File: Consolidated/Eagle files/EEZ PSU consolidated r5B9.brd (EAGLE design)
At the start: 309 x 150 mm, 546 parts, among them IC1 LTC3864EMSE#PBF, IC10 REF5025AIDG4, IC11 DAC8552IDGKTG4, IC12 ADG465SOT-23, IC13 TS5A9411DCKT, IC14 ADS1120IPWR, IC15 LP339D, IC16 LM25575MH/NOPB, IC17 TPD4E002DRLR, IC18 TPD2E001DZDR, IC19 ADUM3160BRWZ, IC2 MC79L05, IC20 TLC5925IDBQR, IC21 Si8641EC-B-IS1, IC22 SI8651EC-B-IS1, IC23 SI8651EC-B-IS1, IC24 LD1117ADT33TR, IC25 Si8641EC-B-IS1, IC26 PCA21125T/Q900/1,1, IC27 AT25256B-SSHL-B, IC28 W5500, IC29 BC857BS, IC3 MC78L05, IC30 TLC555, IC31 SN74LVC2G08DCTR, IC32 TPS3705-33D, IC33 SN74LV1T34DBVR, IC34 SN74LVC2G02DCTR, IC4 LM5574MTX/NOPB, IC5 LP2951SO8, IC6 TL072D, IC7 TL072D, IC8 OP27GSZ, IC9 MCP23S08-E/SO, J1 BS-244DSM-R, J2 BS-244DSM-G, J3 BS-244DSM-B, J4 BS-244DSM-R, J5 BS-244DSM-B, Q1 SUD19P06-60, Q10 MMBT5401, Q11 MMBT5401, Q12 MMBT5551, Q13 MMBT5551, Q14 BSS84P, Q15 2N7002, Q16 MMBT5551, Q17 MMBT5401, Q18 MMBT5551, Q19 MMBT5551, Q2 MMBT5401, Q20 BTA26-600, Q21 BTA26-600, Q22 IRLL014N, Q23 IRLML2246TRPBF, Q24 IRLML2246TRPBF, Q25 IRLML2246TRPBF, Q26 IRLML2246TRPBF, Q27 2N7002, Q28 IRLML2246TRPBF, Q29 2N7002, Q3 2N7002, Q30 2N7002, Q4 IRFP250N, Q5 BC857C, Q6 BC846C, Q7 BCP56-16.115, Q8 IRFR5410, Q9 BCP56-16.115, SW1 A101SYCQ04, SW2 1301.9316, X1 39303035, X10 826629-5, X11 2411-01, X12 MC000006, X13 TSW-113-07-F-D, X14 MC000005, X15 TSW-113-07-F-D, X16 09185067324, X17 22-23-2021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

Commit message: BOM corrections, Q1 gate trace improved
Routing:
- net N$30: track 4.32 -> 0.00 mm
- added copper zone on layer 1, net N$30
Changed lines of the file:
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@@
 <via x="107.2261" y="115.6335" extent="1-16" drill="0.6" shape="square"/>
 <via x="111.2901" y="115.6335" extent="1-16" drill="0.6" shape="square"/>
-<polygon width="0.254" layer="1" isolate="0.3048" thermals="no">
+<polygon width="0.254" layer="1" isolate="0.3048" thermals="no" rank="2">
 <vertex x="105.0925" y="118.364"/>
 <vertex x="112.0775" y="118.364"/>
@@
 <contactref element="Q1" pad="1"/>
 <contactref element="IC1" pad="12"/>
-<wire x1="111.485" y1="113.6523" x2="111.485" y2="113.178" width="0.254" layer="1"/>
-<wire x1="111.485" y1="113.178" x2="111.5695" y2="113.0935" width="0.254" layer="1"/>
-<wire x1="114.6937" y1="111.5695" x2="113.03" y2="111.5695" width="0.6096" layer="1"/>
-<wire x1="111.5695" y1="113.03" x2="113.03" y2="111.5695" width="0.6096" layer="1"/>
-<wire x1="111.5695" y1="113.03" x2="111.5695" y2="113.0935" width="0" layer="19" extent="1-1"/>
+<polygon width="0.254" layer="1" isolate="0.3048" thermals="no">
+<vertex x="111.506" y="114.173"/>
+<vertex x="112.4585" y="114.173"/>
+<vertex x="112.4585" y="113.03"/>
+<vertex x="113.284" y="112.2045"/>
+<vertex x="115.824" y="112.2045"/>
+<vertex x="115.824" y="110.998"/>
+<vertex x="111.506" y="110.998"/>
+</polygon>
 </signal>
 <signal name="N$31">

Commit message: C39 marked as n.c.
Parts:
- C39: value 2u2 -> n.c.
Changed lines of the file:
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@@
 <attribute name="VALUE" x="105.537" y="133.35" size="0.8128" layer="27" ratio="10" rot="R270"/>
 </element>
-<element name="C39" library="rcl" package="C0805" value="2u2" x="98.298" y="129.54" smashed="yes" rot="R270">
+<element name="C39" library="rcl" package="C0805" value="n.c." x="98.298" y="129.54" smashed="yes" rot="R270">
 <attribute name="NAME" x="97.917" y="127.1905" size="1.016" layer="25" ratio="10" rot="R270"/>
 <attribute name="VALUE" x="98.679" y="128.397" size="1.016" layer="27" ratio="10" rot="R90"/>

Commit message: holes removed from outline layer
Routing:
- net D+: vias 2 -> 1
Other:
- board text removed: "Remote programming 1"

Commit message: X18 type changed
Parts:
- X18: value 826629-8 -> MC34753

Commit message: R97 and R102 values swapped
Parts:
- R102: value 5K6 -> 4K7
- R97: value 4K7 -> 5K6
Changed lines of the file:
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@@
 <attribute name="VALUE" x="45.4025" y="144.7165" size="1.016" layer="27" ratio="10" rot="R180"/>
 </element>
-<element name="R102" library="rcl" package="R0805" value="5K6" x="69.9135" y="118.745" smashed="yes" rot="R180">
+<element name="R102" library="rcl" package="R0805" value="4K7" x="69.9135" y="118.745" smashed="yes" rot="R180">
 <attribute name="NAME" x="72.0344" y="118.3259" size="1.016" layer="25" ratio="10"/>
 <attribute name="VALUE" x="68.6054" y="118.2751" size="1.016" layer="27" ratio="10"/>
@@
 <attribute name="VALUE" x="86.6775" y="91.059" size="1.016" layer="27" ratio="10"/>
 </element>
-<element name="R97" library="rcl" package="R0805" value="4K7" x="69.9135" y="116.7765" smashed="yes">
+<element name="R97" library="rcl" package="R0805" value="5K6" x="69.9135" y="116.7765" smashed="yes">
 <attribute name="NAME" x="65.278" y="116.332" size="1.016" layer="25" ratio="10"/>
 <attribute name="VALUE" x="68.3895" y="116.0145" size="1.016" layer="27" ratio="10"/>
@@
 <element name="R123" library="rcl" package="R0805" value="16K" x="83.5025" y="25.527" smashed="yes">
 <attribute name="NAME" x="80.6704" y="26.5811" size="0.8128" layer="25" ratio="10" rot="SR270"/>
-<attribute name="VALUE" x="85.3186" y="25.9334" size="0.9906" layer="27" ratio="10" rot="R180"/>
+<attribute name="VALUE" x="84.8741" y="25.9969" size="0.9906" layer="27" ratio="10" rot="R180"/>
 </element>
 <element name="R124" library="rcl" package="R0805" value="10K" x="72.644" y="28.702" smashed="yes" rot="R180">
@@
 <element name="R121" library="rcl" package="R0805" value="5K6" x="78.613" y="25.5905" smashed="yes" rot="R180">
 <attribute name="NAME" x="76.9874" y="23.5204" size="0.9906" layer="25" ratio="10"/>
-<attribute name="VALUE" x="76.7969" y="25.1206" size="0.9906" layer="27" ratio="10"/>
+<attribute name="VALUE" x="77.3049" y="25.1841" size="0.9906" layer="27" ratio="10"/>
 </element>
 <element name="R126" library="rcl" package="R0805" value="1K8" x="78.613" y="27.559" smashed="yes">
@@
 <element name="IC16" library="EEZ_Lib1" package="SOP65P640X110-17N" value="LM25575MH/NOPB" x="82.423" y="31.6865" smashed="yes">
 <attribute name="NAME" x="86.2584" y="32.2961" size="1.016" layer="25" ratio="10" rot="SR270"/>
-<attribute name="VALUE" x="83.5914" y="35.2298" size="1.016" layer="27" ratio="10" rot="SR270"/>
+<attribute name="VALUE" x="76.0857" y="31.3944" size="1.016" layer="27" ratio="10" rot="SR0"/>
 </element>
 <element name="C88" library="rcl" package="C1210" value="4u7" x="75.946" y="35.8775" smashed="yes" rot="R90">
@@
 <element name="C96" library="rcl" package="C0805" value="180p" x="72.644" y="24.765" smashed="yes" rot="R180">
 <attribute name="NAME" x="71.4375" y="22.606" size="1.016" layer="25" ratio="10"/>
-<attribute name="VALUE" x="70.104" y="24.1935" size="1.27" layer="27"/>
+<attribute name="VALUE" x="70.866" y="24.257" size="1.016" layer="27" ratio="10"/>
 </element>
 <element name="R120" library="rcl" package="R1206" value="10R" x="91.948" y="32.8295" smashed="yes" rot="R90">
@@
 <element name="Q22" library="transistor-power" package="SOT223" value="IRLL014N" x="95.377" y="10.16" smashed="yes" rot="R180">
 <attribute name="NAME" x="97.0915" y="5.5372" size="1.27" layer="25" ratio="10" rot="R180"/>
-<attribute name="VALUE" x="94.7547" y="14.732" size="1.016" layer="27" ratio="10" rot="R270"/>
+<attribute name="VALUE" x="91.8845" y="9.5377" size="1.016" layer="27" ratio="10"/>
 </element>
 <element name="X11" library="con-kycon" package="KUSBVX-BS1N" value="2411-01" x="61.7255" y="59.123" smashed="yes" rot="MR0">
@@
 <element name="IC17" library="EEZ_Lib1" package="SOT50P280X60-5N" value="TPD4E002DRLR" x="87.4395" y="61.6585" smashed="yes" rot="R180">
 <attribute name="NAME" x="85.3821" y="59.1185" size="1.27" layer="25" ratio="10" rot="SR0"/>
-<attribute name="VALUE" x="86.8045" y="64.9224" size="0.8128" layer="27" ratio="10" rot="SR270"/>
+<attribute name="VALUE" x="82.9056" y="61.214" size="0.8128" layer="27" ratio="10" rot="SR0"/>
 </element>
 <element name="IC18" library="EEZ_Lib1" package="SOP192P292X122-4N" value="TPD2E001DZDR" x="62.865" y="64.4525" smashed="yes" rot="R270">
@@
 <element name="IC19" library="MyLib6" package="SOIC-16W" value="ADUM3160BRWZ" x="43.053" y="62.103" smashed="yes" rot="R180">
 <attribute name="NAME" x="32.9311" y="63.373" size="1.27" layer="25" ratio="10" rot="SR0"/>
-<attribute name="VALUE" x="48.7299" y="62.611" size="1.016" layer="27" ratio="10" rot="SR180"/>
+<attribute name="VALUE" x="37.7571" y="61.595" size="1.016" layer="27" ratio="10" rot="SR0"/>
 </element>
 <element name="FB5" library="MyLib6" package="BEAD0603" value="60R@100MHz" x="53.1495" y="55.6895" smashed="yes" rot="R180">
 <attribute name="NAME" x="52.0115" y="53.575" size="1.016" layer="25" ratio="10"/>
-<attribute name="VALUE" x="53.473" y="53.5165" size="0.8128" layer="27" ratio="10" rot="R90"/>
+<attribute name="VALUE" x="51.929" y="55.366" size="0.8128" layer="27" ratio="10"/>
 </element>
 <element name="C100" library="rcl" package="C0603" value="100n" x="50.292" y="58.166" smashed="yes" rot="R90">
@@
 <element name="R122" library="rcl" package="R0805" value="2K2" x="83.5025" y="23.5585" smashed="yes" rot="R180">
 <attribute name="NAME" x="81.7245" y="21.463" size="1.016" layer="25" ratio="10"/>
-<attribute name="VALUE" x="84.1375" y="26.0985" size="1.27" layer="27" rot="R180"/>
+<attribute name="VALUE" x="82.169" y="22.987" size="1.016" layer="27" ratio="10"/>
 </element>
 <element name="R125" library="rcl" package="R0805" value="10K" x="72.644" y="26.7335" smashed="yes">
 <attribute name="NAME" x="69.5325" y="28.6385" size="1.016" layer="25" ratio="10" rot="SR270"/>
-<attribute name="VALUE" x="72.009" y="24.1935" size="1.27" layer="27"/>
+<attribute name="VALUE" x="71.374" y="26.162" size="1.016" layer="27" ratio="10"/>
 </element>
 <element name="R74" library="rcl" package="R0805" value="1K" x="29.845" y="101.1555" smashed="yes" rot="R180">
@@
 <element name="R116" library="rcl" package="R0805" value="49R9" x="89.5985" y="7.4295" smashed="yes" rot="R90">
 <attribute name="NAME" x="90.7415" y="9.398" size="1.016" layer="25" ratio="10" rot="SR270"/>
-<attribute name="VALUE" x="92.1385" y="6.7945" size="1.27" layer="27" rot="R90"/>
+<attribute name="VALUE" x="90.297" y="4.7625" size="1.27" layer="27" rot="R90"/>
 </element>
 <element name="R113" library="rcl" package="R0805" value="49R9" x="89.0905" y="17.145" smashed="yes" rot="R90">
 <attribute name="NAME" x="90.17" y="19.1135" size="1.016" layer="25" ratio="10" rot="SR270"/>
-<attribute name="VALUE" x="91.6305" y="16.51" size="1.27" layer="27" rot="R90"/>
+<attribute name="VALUE" x="88.4555" y="19.05" size="1.27" layer="27" rot="R270"/>
 </element>
 <element name="R166" library="rcl" package="R0805" value="5K1" x="187.96" y="41.402" smashed="yes">
@@
 <element name="R109" library="rcl" package="R2512" value="330R/2W" x="26.8605" y="6.731" smashed="yes" rot="R270">
 <attribute name="NAME" x="24.4475" y="10.922" size="1.016" layer="25" ratio="10"/>
-<attribute name="VALUE" x="23.6855" y="9.271" size="1.27" layer="27" rot="R270"/>
+<attribute name="VALUE" x="26.289" y="10.8585" size="1.27" layer="27" rot="R270"/>
 </element>
 <element name="R111" library="rcl" package="R0805" value="2K2" x="46.101" y="20.6375" smashed="yes" rot="R90">

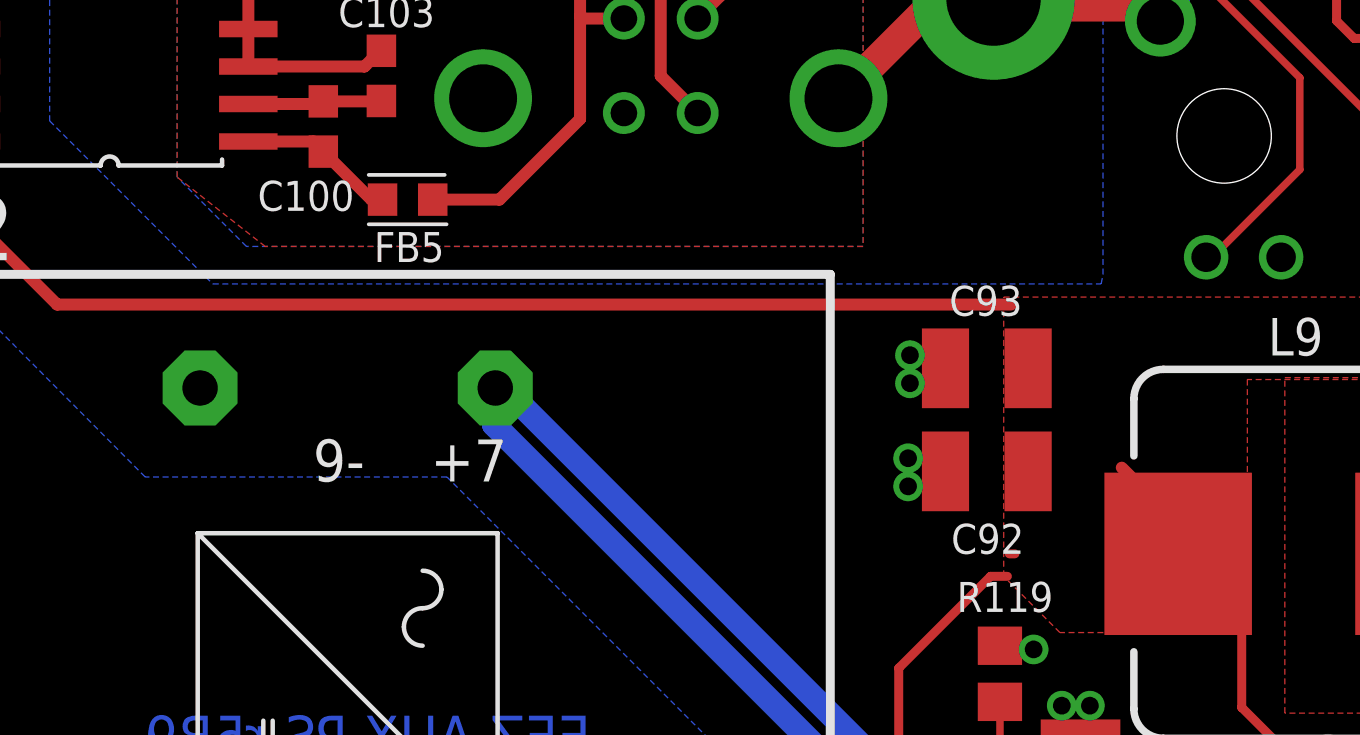
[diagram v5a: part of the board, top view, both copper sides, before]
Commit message: new BOM, added RS and DigiKeyne
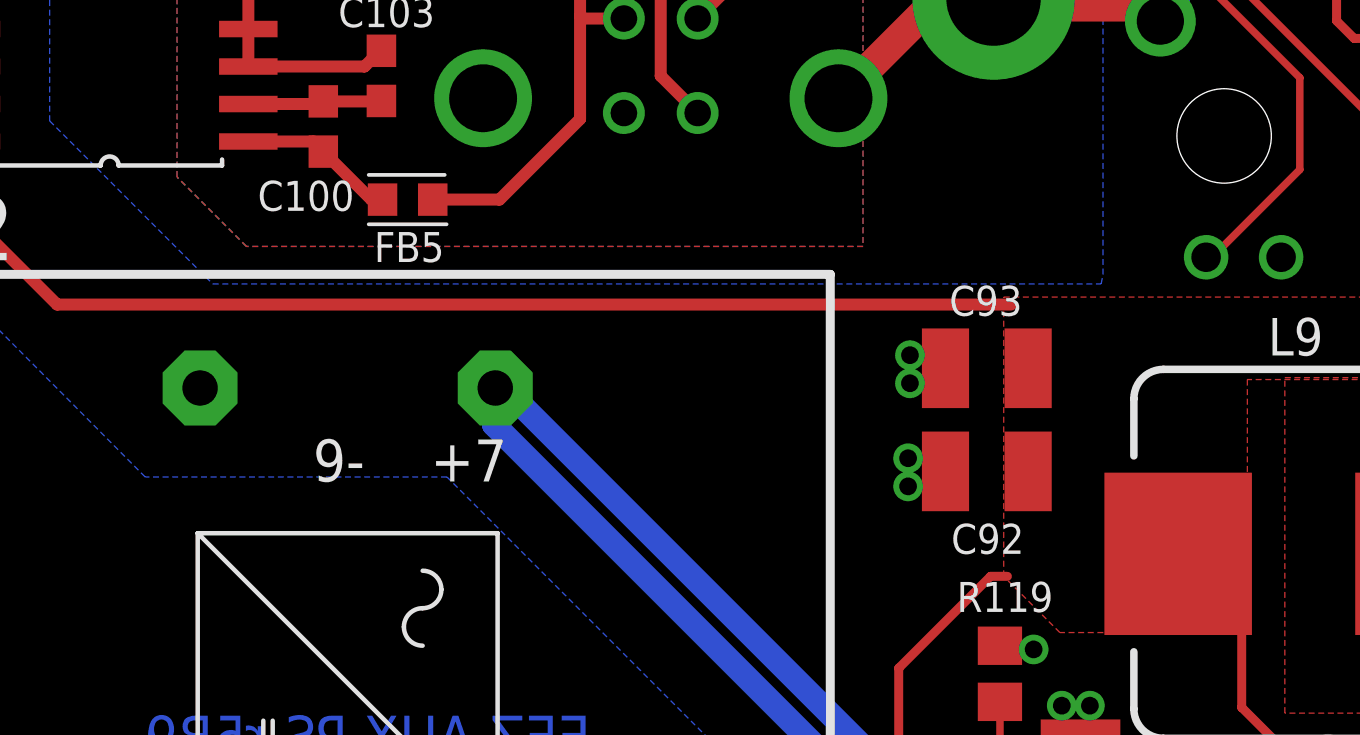
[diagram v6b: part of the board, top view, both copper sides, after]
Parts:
- C1, C2, C3: value 100n -> 4n7/100V
- C105, C108, C110, C112: value 10n -> 4n7/200V
- C106, C111: value UPW1J150MED -> EEEFK1J220P
- C47, C51: value 1n -> 2n2
- Q1: value SUD19P06-60 -> IRFR5305
- X5: value 09185067324 -> 09185107324
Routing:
- net +5V: track 901.8 -> 897.8 mm
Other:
- board text added: "Corrections are marked cyan (Layer 120)"

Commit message: NTC values updated
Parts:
- NTC1: value 10K/Beta:3570K -> NTCS0805E3103JMT
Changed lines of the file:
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@@
 <attribute name="VALUE" x="24.3205" y="125.5395" size="1.016" layer="27" ratio="10" rot="R180"/>
 </element>
-<element name="NTC1" library="EEZ_Lib1" package="R_0204/5+0805" value="10K/Beta:3570K" x="123.1265" y="118.8085" smashed="yes">
+<element name="NTC1" library="EEZ_Lib1" package="R_0204/5+0805" value="NTCS0805E3103JMT" x="123.1265" y="118.8085" smashed="yes">
 <attribute name="NAME" x="121.0945" y="116.1415" size="1.27" layer="25" ratio="10"/>
 <attribute name="VALUE" x="119.126" y="118.491" size="1.016" layer="27" ratio="10"/>
